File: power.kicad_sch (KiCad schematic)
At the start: 16 parts, among them J1 PWR_conn, Q1 2N2222, SW1 Push_button, U9 74HCU04

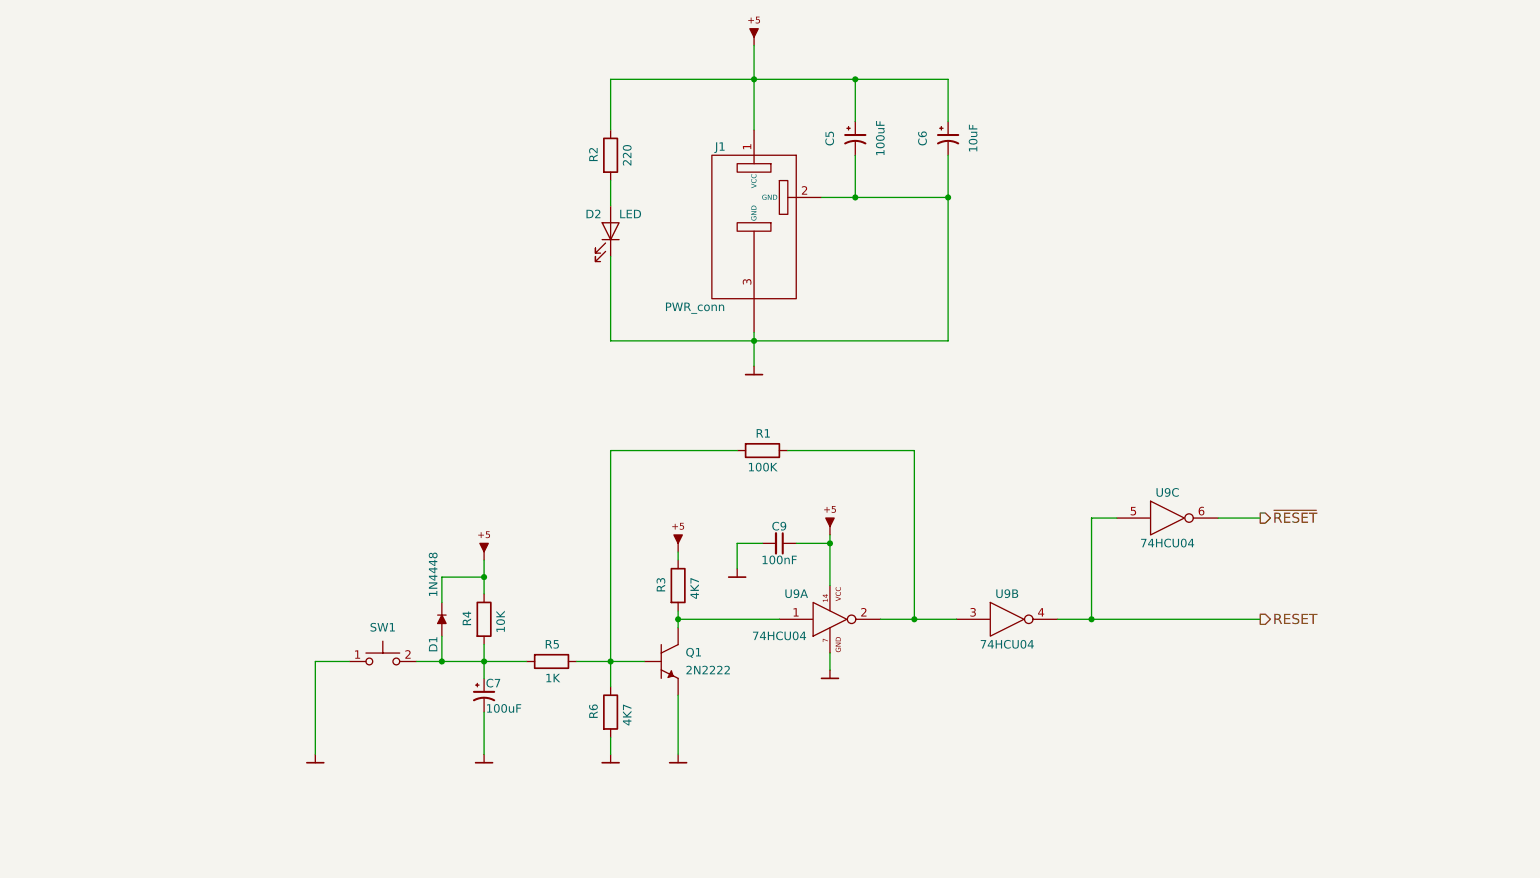
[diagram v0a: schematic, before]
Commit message: Introduce PoR using MIC1232
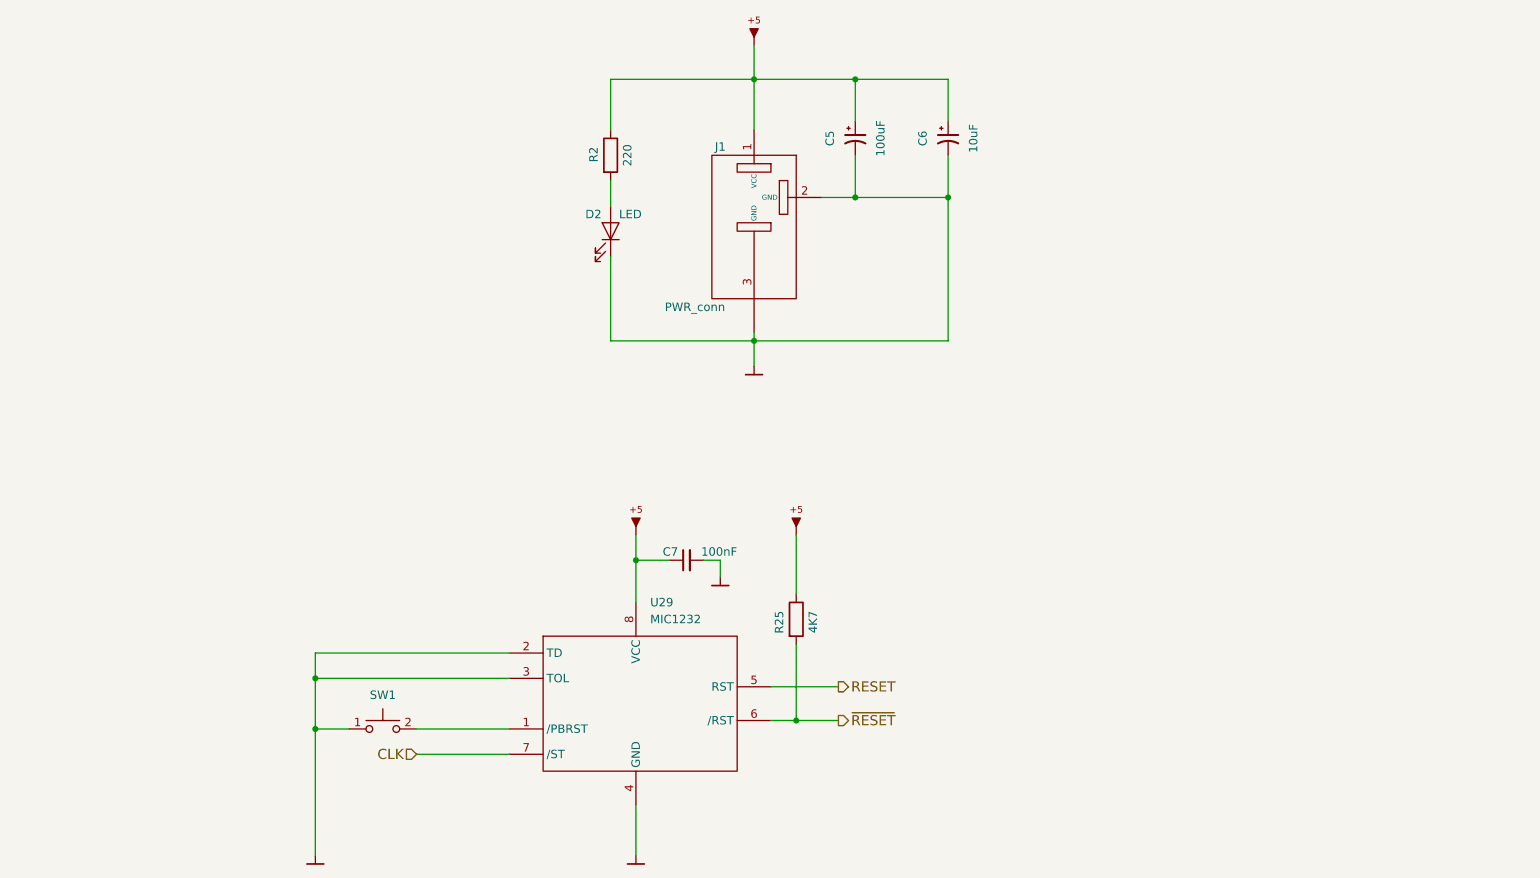
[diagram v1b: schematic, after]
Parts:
- removed C7: 100uF, PCM_artemisa:Radial_capacitor, symbol PCM_artemisa:CP
- removed C9: 100nF, PCM_artemisa:Disc_capacitor, symbol PCM_artemisa:Cap
- removed D1: 1N4448, PCM_artemisa:Axial_diode, symbol PCM_artemisa:1N4448
- removed Q1: 2N2222, PCM_artemisa:TO92, symbol PCM_artemisa:2N2222
- removed R1: 100K, PCM_artemisa:Axial_resistor, symbol PCM_artemisa:R
- removed R3, R6: 4K7, PCM_artemisa:Axial_resistor, symbol PCM_artemisa:R
- removed R4: 10K, PCM_artemisa:Axial_resistor, symbol PCM_artemisa:R
- removed R5: 1K, PCM_artemisa:Axial_resistor, symbol PCM_artemisa:R
- removed U9: 74HCU04, PCM_artemisa:DIP-14_300, symbol PCM_artemisa:74HCU04
- added C7: 100nF, PCM_artemisa:Disc_capacitor, symbol PCM_artemisa:Cap
- added R25: 4K7, PCM_artemisa:Axial_resistor, symbol PCM_artemisa:R
- added U29: MIC1232, symbol PCM_artemisa:MIC1232
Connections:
- net GND: now also C7.2, U29.2 (TD), U29.3 (TOL), U29.4 (GND)
- net RESET: now also U29.5 (RST)
- net VCC: now also C7.1, R25.1, U29.8 (VCC)
- net ~{RESET}: now also R25.2, U29.6 (/RST)
- net at SW1.2: now also U29.1 (/PBRST)
- new net CLK: U29.7 (/ST)

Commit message: Prepare schematic for JST power input
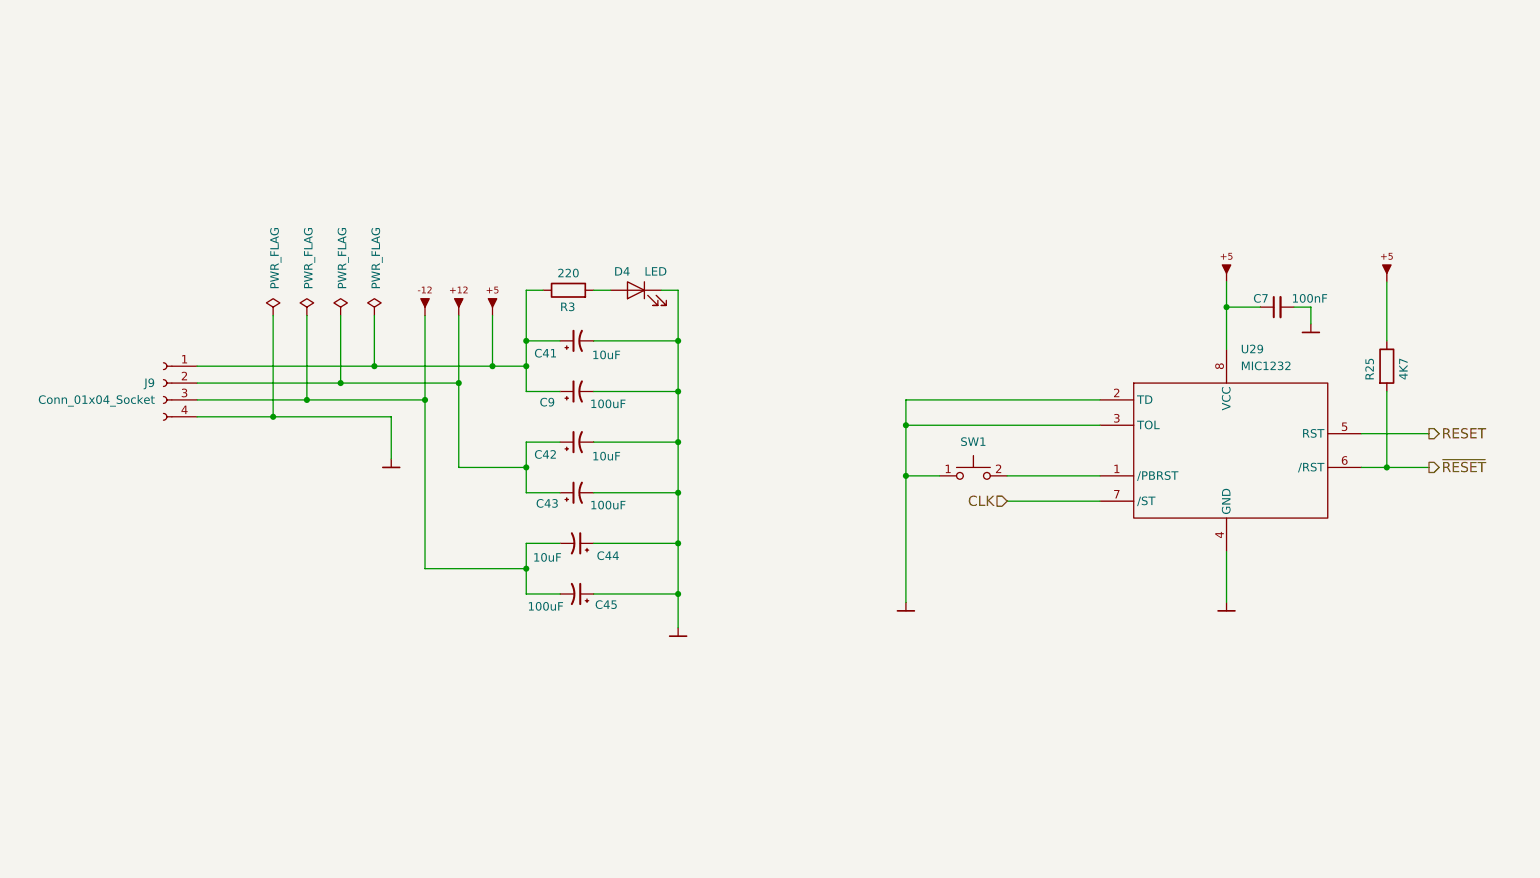
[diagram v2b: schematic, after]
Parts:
- removed C5: 100uF, PCM_artemisa:Radial_capacitor, symbol PCM_artemisa:CP
- removed C6: 10uF, PCM_artemisa:Radial_capacitor, symbol PCM_artemisa:CP
- removed D2: LED, PCM_artemisa:LED, symbol PCM_artemisa:LED
- removed J1: PWR_conn, PCM_artemisa:Jack_55_21, symbol PCM_artemisa:PWR_conn
- removed R2: 220, PCM_artemisa:Axial_resistor, symbol PCM_artemisa:R
- added C41, C42, C44: 10uF, PCM_artemisa:Radial_capacitor, symbol PCM_artemisa:CP
- added C43, C45, C9: 100uF, PCM_artemisa:Radial_capacitor, symbol PCM_artemisa:CP
- added D4: LED, PCM_artemisa:LED, symbol PCM_artemisa:LED
- added J9: Conn_01x04_Socket, symbol Connector:Conn_01x04_Socket
- added R3: 220, PCM_artemisa:Axial_resistor, symbol PCM_artemisa:R
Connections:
- net GND: now also C41.2, C42.2, C43.2, C44.1, C45.1, C9.2, D4.2 (K), J9.4 (Pin_4)
- net VCC: now also C41.1, C9.1, J9.1 (Pin_1), R3.1
- new net: D4.1 (A), R3.2
- new net -12V: C44.2, C45.2, J9.3 (Pin_3)
- new net 12V: C42.1, C43.1, J9.2 (Pin_2)
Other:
- moved on the sheet: C7, R25, SW1, U29

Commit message: Re-annotate the whole schematic
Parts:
- renumbered C41 to C21, C9 to C22, C42 to C23, C43 to C24, C44 to C25, C45 to C26, C7 to C27, D4 to D1, J9 to J2, R3 to R1, R25 to R2, U29 to U20
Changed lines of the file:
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@@
 		(in_pos_files yes)
 		(dnp no)
-		(property "Reference" "#PWR030"
+		(property "Reference" "#PWR082"
 			(at 209.55 68.58 0)
 			(hide yes)
@@
 			(project "motherboard-hk10"
 				(path "/e63e39d7-6ac0-4ffd-8aa3-1841a4541b55/00000000-0000-0000-0000-00005ae11ec9"
-					(reference "#PWR030")
+					(reference "#PWR082")
 					(unit 1)
 				)
@@
 		(in_pos_files yes)
 		(dnp no)
-		(property "Reference" "#PWR023"
+		(property "Reference" "#PWR084"
 			(at 222.25 76.2 0)
 			(hide yes)
@@
 			(project "motherboard-hk10"
 				(path "/e63e39d7-6ac0-4ffd-8aa3-1841a4541b55/00000000-0000-0000-0000-00005ae11ec9"
-					(reference "#PWR023")
+					(reference "#PWR084")
 					(unit 1)
 				)
@@
 		(in_pos_files yes)
 		(dnp no)
-		(property "Reference" "#PWR031"
+		(property "Reference" "#PWR085"
 			(at 233.68 68.58 0)
 			(hide yes)
@@
 			(project "motherboard-hk10"
 				(path "/e63e39d7-6ac0-4ffd-8aa3-1841a4541b55/00000000-0000-0000-0000-00005ae11ec9"
-					(reference "#PWR031")
+					(reference "#PWR085")
 					(unit 1)
 				)
@@
 		(dnp no)
 		(fields_autoplaced yes)
-		(property "Reference" "#PWR026"
+		(property "Reference" "#PWR078"
 			(at 93.98 73.66 0)
 			(hide yes)
@@
 			(project "motherboard-hk10"
 				(path "/e63e39d7-6ac0-4ffd-8aa3-1841a4541b55/00000000-0000-0000-0000-00005ae11ec9"
-					(reference "#PWR026")
+					(reference "#PWR078")
 					(unit 1)
 				)
@@
 		(in_pos_files yes)
 		(dnp no)
-		(property "Reference" "#FLG03"
+		(property "Reference" "#FLG02"
 			(at 71.12 70.485 0)
 			(hide yes)
@@
 			(project "motherboard-hk10"
 				(path "/e63e39d7-6ac0-4ffd-8aa3-1841a4541b55/00000000-0000-0000-0000-00005ae11ec9"
-					(reference "#FLG03")
+					(reference "#FLG02")
 					(unit 1)
 				)
@@
 		(dnp no)
 		(fields_autoplaced yes)
-		(property "Reference" "U29"
+		(property "Reference" "U20"
 			(at 211.6933 77.47 0)
 			(show_name no)
@@
 			(project "motherboard-hk10"
 				(path "/e63e39d7-6ac0-4ffd-8aa3-1841a4541b55/00000000-0000-0000-0000-00005ae11ec9"
-					(reference "U29")
+					(reference "U20")
 					(unit 1)
 				)
@@
 		(in_pos_files yes)
 		(dnp no)
-		(property "Reference" "#FLG02"
+		(property "Reference" "#FLG03"
 			(at 76.2 70.485 0)
 			(hide yes)
@@
 			(project "motherboard-hk10"
 				(path "/e63e39d7-6ac0-4ffd-8aa3-1841a4541b55/00000000-0000-0000-0000-00005ae11ec9"
-					(reference "#FLG02")
+					(reference "#FLG03")
 					(unit 1)
 				)
@@
 		(in_pos_files yes)
 		(dnp no)
-		(property "Reference" "C7"
+		(property "Reference" "C27"
 			(at 215.9 69.85 90)
 			(show_name no)
@@
 			(project "motherboard-hk10"
 				(path "/e63e39d7-6ac0-4ffd-8aa3-1841a4541b55/00000000-0000-0000-0000-00005ae11ec9"
-					(reference "C7")
+					(reference "C27")
 					(unit 1)
 				)
@@
 		(in_pos_files yes)
 		(dnp no)
-		(property "Reference" "J9"
+		(property "Reference" "J2"
 			(at 48.26 82.5499 0)
 			(show_name no)
@@
 			(project "motherboard-hk10"
 				(path "/e63e39d7-6ac0-4ffd-8aa3-1841a4541b55/00000000-0000-0000-0000-00005ae11ec9"
-					(reference "J9")
+					(reference "J2")
 					(unit 1)
 				)
@@
 		(dnp no)
 		(fields_autoplaced yes)
-		(property "Reference" "#PWR027"
+		(property "Reference" "#PWR077"
 			(at 88.9 73.66 0)
 			(hide yes)
@@
 			(project "motherboard-hk10"
 				(path "/e63e39d7-6ac0-4ffd-8aa3-1841a4541b55/00000000-0000-0000-0000-00005ae11ec9"
-					(reference "#PWR027")
+					(reference "#PWR077")
 					(unit 1)
 				)
@@
 		(in_pos_files yes)
 		(dnp no)
-		(property "Reference" "C43"
+		(property "Reference" "C24"
 			(at 107.315 100.711 90)
 			(show_name no)
@@
 			(project "motherboard-hk10"
 				(path "/e63e39d7-6ac0-4ffd-8aa3-1841a4541b55/00000000-0000-0000-0000-00005ae11ec9"
-					(reference "C43")
+					(reference "C24")
 					(unit 1)
 				)
@@
 		(in_pos_files yes)
 		(dnp no)
-		(property "Reference" "C45"
+		(property "Reference" "C26"
 			(at 116.205 115.951 90)
 			(show_name no)
@@
 			(project "motherboard-hk10"
 				(path "/e63e39d7-6ac0-4ffd-8aa3-1841a4541b55/00000000-0000-0000-0000-00005ae11ec9"
-					(reference "C45")
+					(reference "C26")
 					(unit 1)
 				)
@@
 		(in_pos_files yes)
 		(dnp no)
-		(property "Reference" "#FLG01"
+		(property "Reference" "#FLG04"
 			(at 81.28 70.485 0)
 			(hide yes)
@@
 			(project "motherboard-hk10"
 				(path "/e63e39d7-6ac0-4ffd-8aa3-1841a4541b55/00000000-0000-0000-0000-00005ae11ec9"
-					(reference "#FLG01")
+					(reference "#FLG04")
 					(unit 1)
 				)
@@
 		(in_pos_files yes)
 		(dnp no)
-		(property "Reference" "C9"
+		(property "Reference" "C22"
 			(at 107.315 85.471 90)
 			(show_name no)
@@
 			(project "motherboard-hk10"
 				(path "/e63e39d7-6ac0-4ffd-8aa3-1841a4541b55/00000000-0000-0000-0000-00005ae11ec9"
-					(reference "C9")
+					(reference "C22")
 					(unit 1)
 				)
@@
 		(in_pos_files yes)
 		(dnp no)
-		(property "Reference" "R25"
+		(property "Reference" "R2"
 			(at 231.14 78.74 0)
 			(show_name no)
@@
 			(project "motherboard-hk10"
 				(path "/e63e39d7-6ac0-4ffd-8aa3-1841a4541b55/00000000-0000-0000-0000-00005ae11ec9"
-					(reference "R25")
+					(reference "R2")
 					(unit 1)
 				)
@@
 		(in_pos_files yes)
 		(dnp no)
-		(property "Reference" "C41"
+		(property "Reference" "C21"
 			(at 107.061 78.105 90)
 			(show_name no)
@@
 			(project "motherboard-hk10"
 				(path "/e63e39d7-6ac0-4ffd-8aa3-1841a4541b55/00000000-0000-0000-0000-00005ae11ec9"
-					(reference "C41")
+					(reference "C21")
 					(unit 1)
 				)
@@
 		(in_pos_files yes)
 		(dnp no)
-		(property "Reference" "#PWR024"
+		(property "Reference" "#PWR079"
 			(at 99.06 73.66 0)
 			(hide yes)
@@
 			(project "motherboard-hk10"
 				(path "/e63e39d7-6ac0-4ffd-8aa3-1841a4541b55/00000000-0000-0000-0000-00005ae11ec9"
-					(reference "#PWR024")
+					(reference "#PWR079")
 					(unit 1)
 				)
@@
 		(in_pos_files yes)
 		(dnp no)
-		(property "Reference" "#PWR025"
+		(property "Reference" "#PWR081"
 			(at 161.29 118.11 0)
 			(hide yes)
@@
 			(project "motherboard-hk10"
 				(path "/e63e39d7-6ac0-4ffd-8aa3-1841a4541b55/00000000-0000-0000-0000-00005ae11ec9"
-					(reference "#PWR025")
+					(reference "#PWR081")
 					(unit 1)
 				)
@@
 		(in_pos_files yes)
 		(dnp no)
-		(property "Reference" "C42"
+		(property "Reference" "C23"
 			(at 107.061 93.345 90)
 			(show_name no)
@@
 			(project "motherboard-hk10"
 				(path "/e63e39d7-6ac0-4ffd-8aa3-1841a4541b55/00000000-0000-0000-0000-00005ae11ec9"
-					(reference "C42")
+					(reference "C23")
 					(unit 1)
 				)
@@
 		(in_pos_files yes)
 		(dnp no)
-		(property "Reference" "D4"
+		(property "Reference" "D1"
 			(at 117.348 65.786 0)
 			(show_name no)
@@
 			(project "motherboard-hk10"
 				(path "/e63e39d7-6ac0-4ffd-8aa3-1841a4541b55/00000000-0000-0000-0000-00005ae11ec9"
-					(reference "D4")
+					(reference "D1")
 					(unit 1)
 				)
@@
 		(in_pos_files yes)
 		(dnp no)
-		(property "Reference" "#FLG04"
+		(property "Reference" "#FLG01"
 			(at 66.04 70.485 0)
 			(hide yes)
@@
 			(project "motherboard-hk10"
 				(path "/e63e39d7-6ac0-4ffd-8aa3-1841a4541b55/00000000-0000-0000-0000-00005ae11ec9"
-					(reference "#FLG04")
+					(reference "#FLG01")
 					(unit 1)
 				)
@@
 		(in_pos_files yes)
 		(dnp no)
-		(property "Reference" "C44"
+		(property "Reference" "C25"
 			(at 116.459 108.585 90)
 			(show_name no)
@@
 			(project "motherboard-hk10"
 				(path "/e63e39d7-6ac0-4ffd-8aa3-1841a4541b55/00000000-0000-0000-0000-00005ae11ec9"
-					(reference "C44")
+					(reference "C25")
 					(unit 1)
 				)
@@
 		(in_pos_files yes)
 		(dnp no)
-		(property "Reference" "#PWR033"
+		(property "Reference" "#PWR076"
 			(at 83.82 96.52 0)
 			(hide yes)
@@
 			(project "motherboard-hk10"
 				(path "/e63e39d7-6ac0-4ffd-8aa3-1841a4541b55/00000000-0000-0000-0000-00005ae11ec9"
-					(reference "#PWR033")
+					(reference "#PWR076")
 					(unit 1)
 				)
@@
 		(in_pos_files yes)
 		(dnp no)
-		(property "Reference" "#PWR034"
+		(property "Reference" "#PWR080"
 			(at 127 121.92 0)
 			(hide yes)
@@
 			(project "motherboard-hk10"
 				(path "/e63e39d7-6ac0-4ffd-8aa3-1841a4541b55/00000000-0000-0000-0000-00005ae11ec9"
-					(reference "#PWR034")
+					(reference "#PWR080")
 					(unit 1)
 				)
@@
 		(in_pos_files yes)
 		(dnp no)
-		(property "Reference" "#PWR032"
+		(property "Reference" "#PWR083"
 			(at 209.55 118.11 0)
 			(hide yes)
@@
 			(project "motherboard-hk10"
 				(path "/e63e39d7-6ac0-4ffd-8aa3-1841a4541b55/00000000-0000-0000-0000-00005ae11ec9"
-					(reference "#PWR032")
+					(reference "#PWR083")
 					(unit 1)
 				)
@@
 		(in_pos_files yes)
 		(dnp no)
-		(property "Reference" "R3"
+		(property "Reference" "R1"
 			(at 109.22 71.12 0)
 			(show_name no)
@@
 			(project "motherboard-hk10"
 				(path "/e63e39d7-6ac0-4ffd-8aa3-1841a4541b55/00000000-0000-0000-0000-00005ae11ec9"
-					(reference "R3")
-					(unit 1)
-				)
+					(reference "R1")
+					(unit 1)
+				)
